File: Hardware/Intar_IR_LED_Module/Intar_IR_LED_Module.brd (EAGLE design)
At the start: 25.8 x 22.4 mm, 19 parts, among them J1 GROVE-4P-2.0-3470130P1, Q1 MMBT2222A, Q2 MMBT2222A

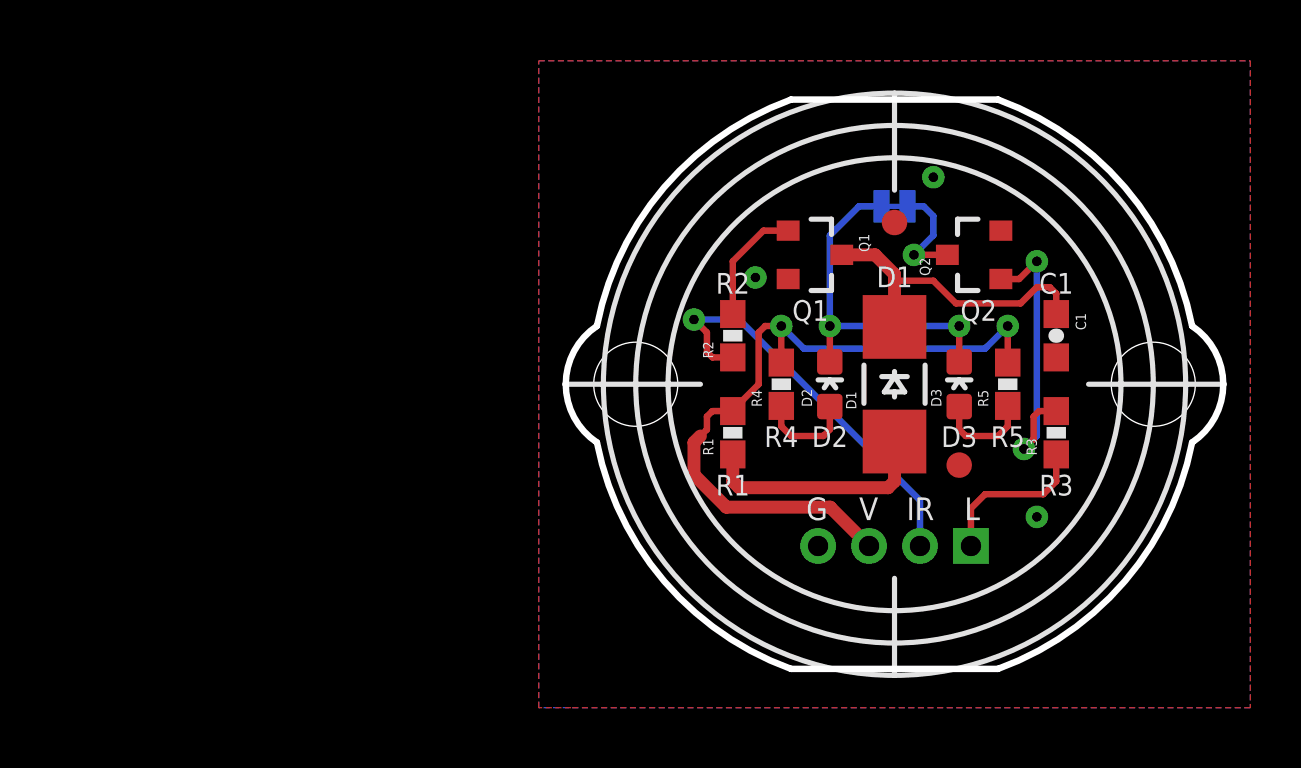
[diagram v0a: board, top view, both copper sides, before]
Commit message: Re-constructed board outline for IR LED Module.
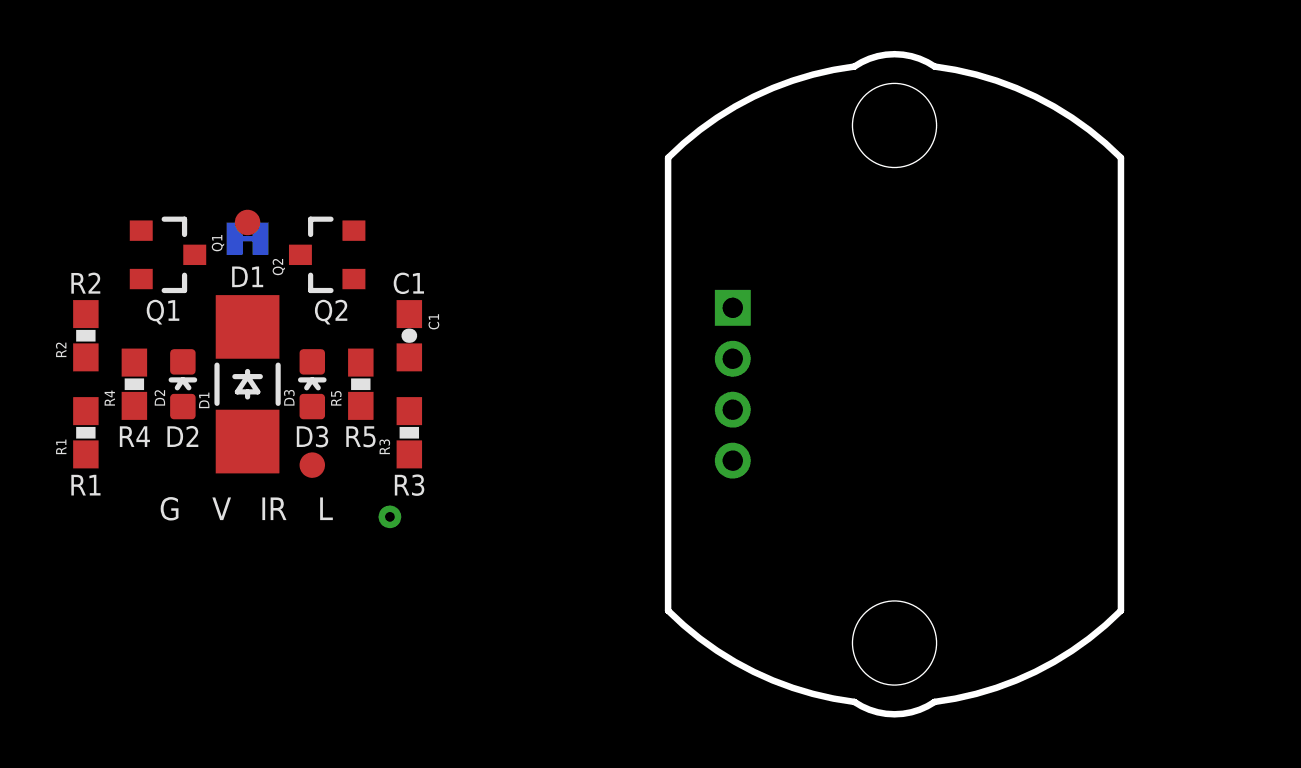
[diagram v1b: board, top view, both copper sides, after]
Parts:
- moved LOGO1 39.4 mm to (-46.4, -4.32)
- moved SJ1 25.4 mm to (-25.4, 5.71)
- moved D2 25.4 mm to (-27.9, 0.00)
- moved Q2 25.4 mm to (-22.2, 5.08)
- moved C1 25.4 mm to (-19.1, 1.91)
- moved D1 25.4 mm to (-25.4, 0.00)
- moved D3 25.4 mm to (-22.9, 0.00)
- moved FID1 25.4 mm to (-25.4, 6.35)
- moved FID2 25.4 mm to (-22.9, -3.17)
- moved Q1 25.4 mm to (-28.6, 5.08)
- moved R1 25.4 mm to (-31.8, -1.91)
- moved R2 25.4 mm to (-31.8, 1.91)
- moved R3 25.4 mm to (-19.1, -1.91)
- moved R4 25.4 mm to (-29.8, 0.00)
- moved R5 25.4 mm to (-21.0, 0.00)
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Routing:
- net VCC: track 28.6 -> 0.00 mm, vias 2 -> 0
- net IR: track 16.2 -> 0.00 mm, vias 1 -> 0
- net N$4: track 14.0 -> 0.00 mm, vias 2 -> 0
- net N$3: track 12.3 -> 0.00 mm
- net N$5: track 11.7 -> 0.00 mm, vias 2 -> 0
- net N$2: track 9.18 -> 0.00 mm
- net LEDS: track 6.32 -> 0.00 mm
- net N$1: track 4.74 -> 0.00 mm
- net N$8: track 4.33 -> 0.00 mm, vias 1 -> 0
- net N$7: track 3.87 -> 0.00 mm
- net N$6: track 3.87 -> 0.00 mm
- removed copper zone on layer 1, net GND
- removed copper zone on layer 16, net GND
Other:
- board size 25.8 x 22.4 mm -> 17.8 x 25.9 mm
